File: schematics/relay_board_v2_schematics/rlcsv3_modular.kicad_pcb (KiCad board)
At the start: 2 copper layers, 45 x 75 mm, 46 parts, among them J1 Programming Header, Q1 MMBF170, Q2 MMBF170, U1 SPST_POWER_RELAY, U2 PIC16F1826-ISO, U3 dpdt_relay, U4 INA180A1, U5 CONN_01x05, U6 INA180A1, U7 CONN_01x05

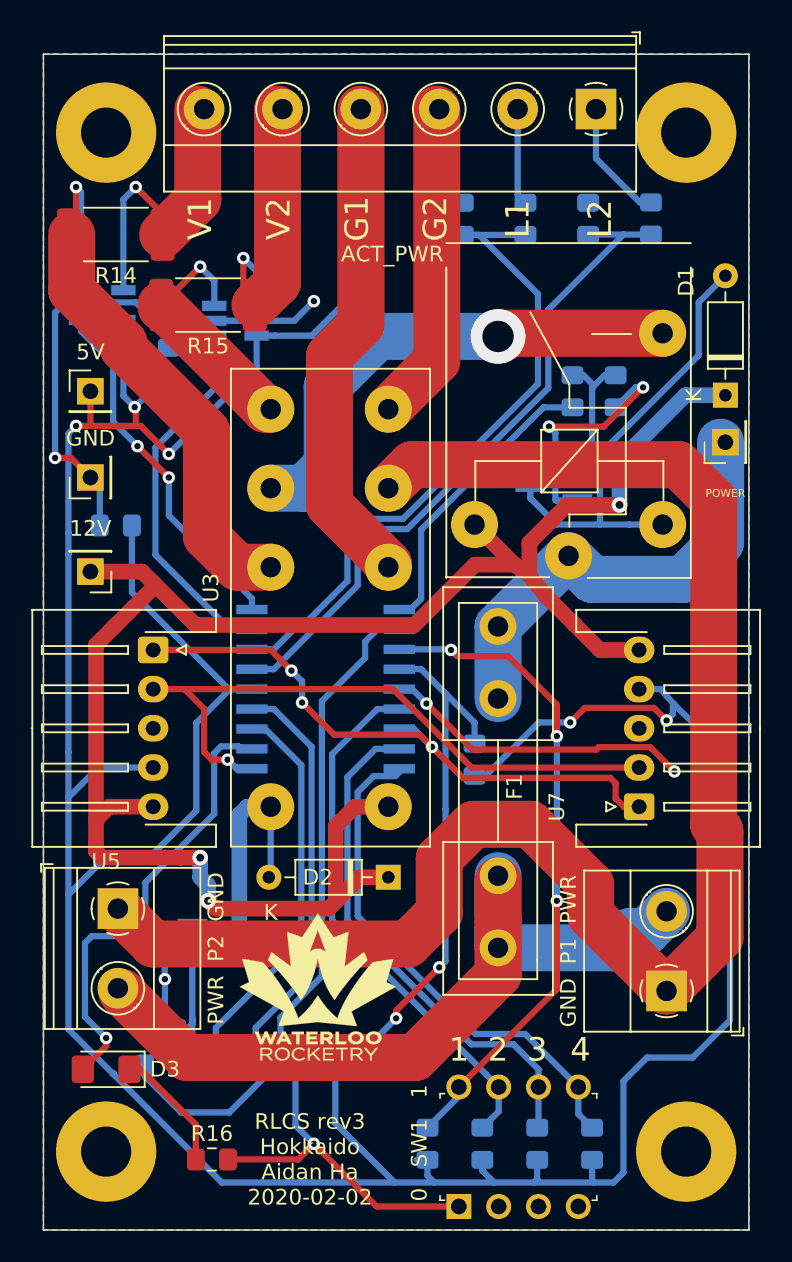
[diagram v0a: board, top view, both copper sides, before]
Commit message: Add nitpick changes. Add Gerbers
Signed-off-by: AIDAN HA <qbha@edu.uwaterloo.ca>
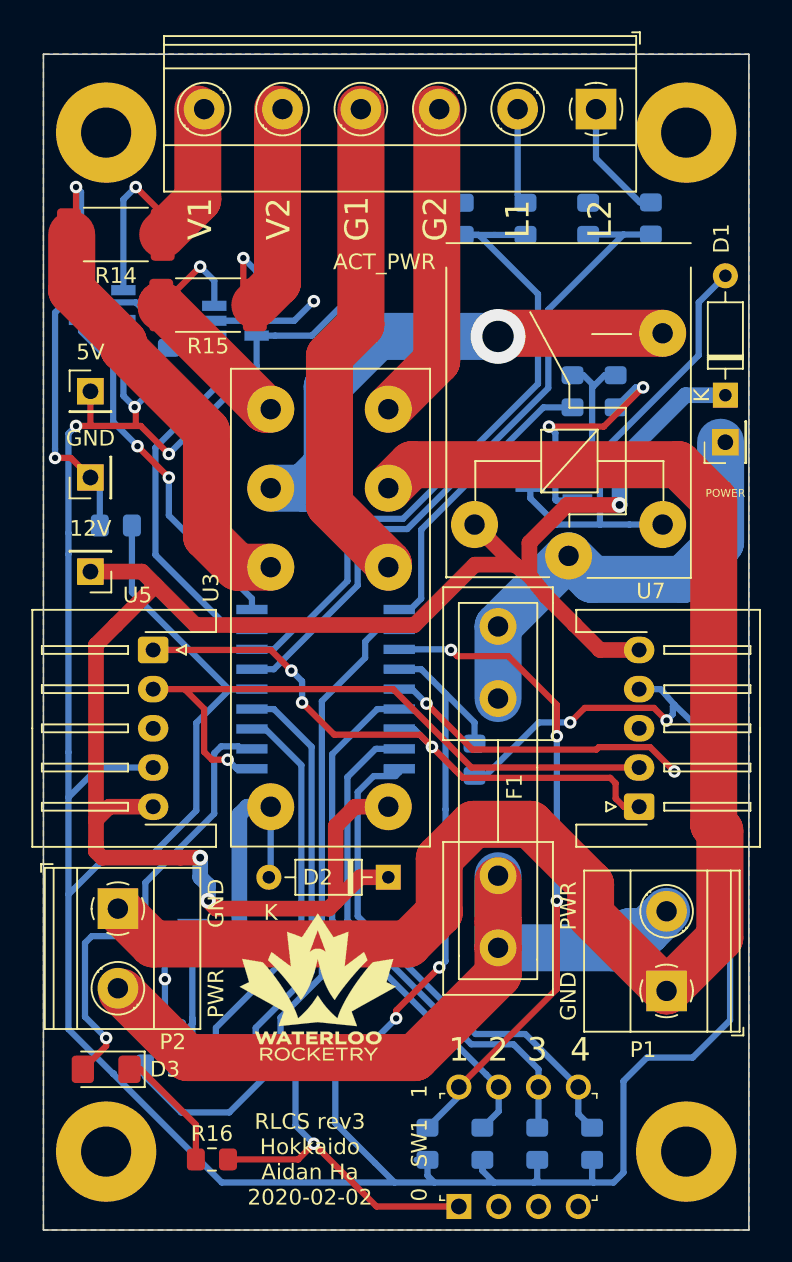
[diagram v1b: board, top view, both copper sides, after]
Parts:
- GND      PWR: renamed from GND  P1  PWR
- PWR      GND: renamed from PWR  P2  GND
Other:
- board text added: "P1"
- board text added: "P2"
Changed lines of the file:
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@@
   (general
     (thickness 1.6)
-    (drawings 18)
+    (drawings 20)
     (tracks 471)
     (zones 0)
@@
     (descr "Terminal Block Phoenix MKDS-1,5-2-5.08, 2 pins, pitch 5.08mm, size 10.2x9.8mm^2, drill diamater 1.3mm, pad diameter 2.6mm, see http://www.farnell.com/datasheets/100425.pdf, script-generated using https://github.com/pointhi/kicad-footprint-generator/scripts/TerminalBlock_Phoenix")
     (tags "THT Terminal Block Phoenix MKDS-1,5-2-5.08 pitch 5.08mm size 10.2x9.8mm^2 drill 1.3mm pad 2.6mm")
-    (fp_text reference "PWR  P2  GND" (at 2.54 -6.26 90) (layer F.SilkS)
+    (fp_text reference "PWR      GND" (at 2.54 -6.26 90) (layer F.SilkS)
       (effects (font (size 1 1) (thickness 0.15)))
     )
@@
     (descr "Terminal Block Phoenix MKDS-1,5-6, 6 pins, pitch 5mm, size 30x9.8mm^2, drill diamater 1.3mm, pad diameter 2.6mm, see http://www.farnell.com/datasheets/100425.pdf, script-generated using https://github.com/pointhi/kicad-footprint-generator/scripts/TerminalBlock_Phoenix")
     (tags "THT Terminal Block Phoenix MKDS-1,5-6 pitch 5mm size 30x9.8mm^2 drill 1.3mm pad 2.6mm")
-    (fp_text reference ACT_PWR (at 13 -9.25) (layer F.SilkS)
+    (fp_text reference ACT_PWR (at 13.5 -9.75) (layer F.SilkS)
       (effects (font (size 1 1) (thickness 0.15)))
     )
@@
     (descr "JST XH series connector, S5B-XH-A-1 (http://www.jst-mfg.com/product/pdf/eng/eXH.pdf), generated with kicad-footprint-generator")
     (tags "connector JST XH horizontal")
-    (fp_text reference U5 (at 13.5 3) (layer F.SilkS)
+    (fp_text reference U5 (at -3.5 1) (layer F.SilkS)
       (effects (font (size 1 1) (thickness 0.15)))
     )
@@
     (descr "Diode, DO-35_SOD27 series, Axial, Horizontal, pin pitch=7.62mm, , length*diameter=4*2mm^2, , http://www.diodes.com/_files/packages/DO-35.pdf")
     (tags "Diode DO-35_SOD27 series Axial Horizontal pin pitch 7.62mm  length 4mm diameter 2mm")
-    (fp_text reference D1 (at 7.25 -2.5 270) (layer F.SilkS)
+    (fp_text reference D1 (at 10 -0.25 270) (layer F.SilkS)
       (effects (font (size 1 1) (thickness 0.15)))
     )
@@
       (effects (font (size 1 1) (thickness 0.15)))
     )
-    (fp_text user K (at 0 -2 90) (layer F.SilkS)
+    (fp_text user K (at 0 -1.5 90) (layer F.SilkS)
       (effects (font (size 1 1) (thickness 0.15)))
     )
@@
     (descr "Terminal Block Phoenix MKDS-1,5-2-5.08, 2 pins, pitch 5.08mm, size 10.2x9.8mm^2, drill diamater 1.3mm, pad diameter 2.6mm, see http://www.farnell.com/datasheets/100425.pdf, script-generated using https://github.com/pointhi/kicad-footprint-generator/scripts/TerminalBlock_Phoenix")
     (tags "THT Terminal Block Phoenix MKDS-1,5-2-5.08 pitch 5.08mm size 10.2x9.8mm^2 drill 1.3mm pad 2.6mm")
-    (fp_text reference "GND  P1  PWR" (at 2.54 -6.26 90) (layer F.SilkS)
+    (fp_text reference "GND      PWR" (at 2.54 -6.26 90) (layer F.SilkS)
       (effects (font (size 1 1) (thickness 0.15)))
     )
@@
     (descr "JST XH series connector, S5B-XH-A-1 (http://www.jst-mfg.com/product/pdf/eng/eXH.pdf), generated with kicad-footprint-generator")
     (tags "connector JST XH horizontal")
-    (fp_text reference U7 (at 0 -5.25 90) (layer F.SilkS)
+    (fp_text reference U7 (at 13.75 0.75 180) (layer F.SilkS)
       (effects (font (size 1 1) (thickness 0.15)))
     )
@@
     )
   )
-  (gr_text "12V 5V GND SCL SDA" (at 165.25 112 270) (layer B.SilkS)
-    (effects (font (size 0.8 0.8) (thickness 0.15)))
+  (gr_text "P2\n" (at 138.25 132) (layer F.SilkS)
+    (effects (font (size 1 1) (thickness 0.15)))
+  )
+  (gr_text P1 (at 168.25 132.5) (layer F.SilkS)
+    (effects (font (size 1 1) (thickness 0.15)))
+  )
+  (gr_text "12V 5V GND SCL SDA" (at 170.25 111.75 270) (layer B.SilkS)
+    (effects (font (size 0.8 0.8) (thickness 0.15)) (justify mirror))
   )
   (gr_text "12V 5V GND SCL SDA" (at 134.75 111.75 90) (layer B.SilkS)
-    (effects (font (size 0.8 0.8) (thickness 0.15)))
+    (effects (font (size 0.8 0.8) (thickness 0.15)) (justify mirror))
   )
   (gr_text "~MCLR 5V" (at 154 133.25 90) (layer B.SilkS)
